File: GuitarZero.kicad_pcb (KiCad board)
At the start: 6 copper layers, 160.4 x 102.9 mm, 144 parts, among them J1 USB_A, J2 USB_B_Micro, J3 AudioJack3_SwitchT, J4 MCU_Debug, J6 Micro_SD_Card_Det_Hirose_DM3AT, SW1 SW_Push, SW2 SW_Push, SW3 SW_Push, SW4 SW_Push, SW5 SW_Push, SW6 SW_Push, U1 TPS54325, U10 FPGA_GPIO_Extra, U11 5x7 LED_matrix, U12 MCU_GPIO_Extra, U13 5x7 LED_matrix, U14 Power_Jumpers, U2 TSP54294, U3 XC7A100T-FTG256, U4 EFM32GG332, U5 S25FL127S, U6 Oscillator, U7 FPGA_JTAG_Debug, U8 PCM1754, U9 TPD_Current_Switch, Y1 Crystal_GND23

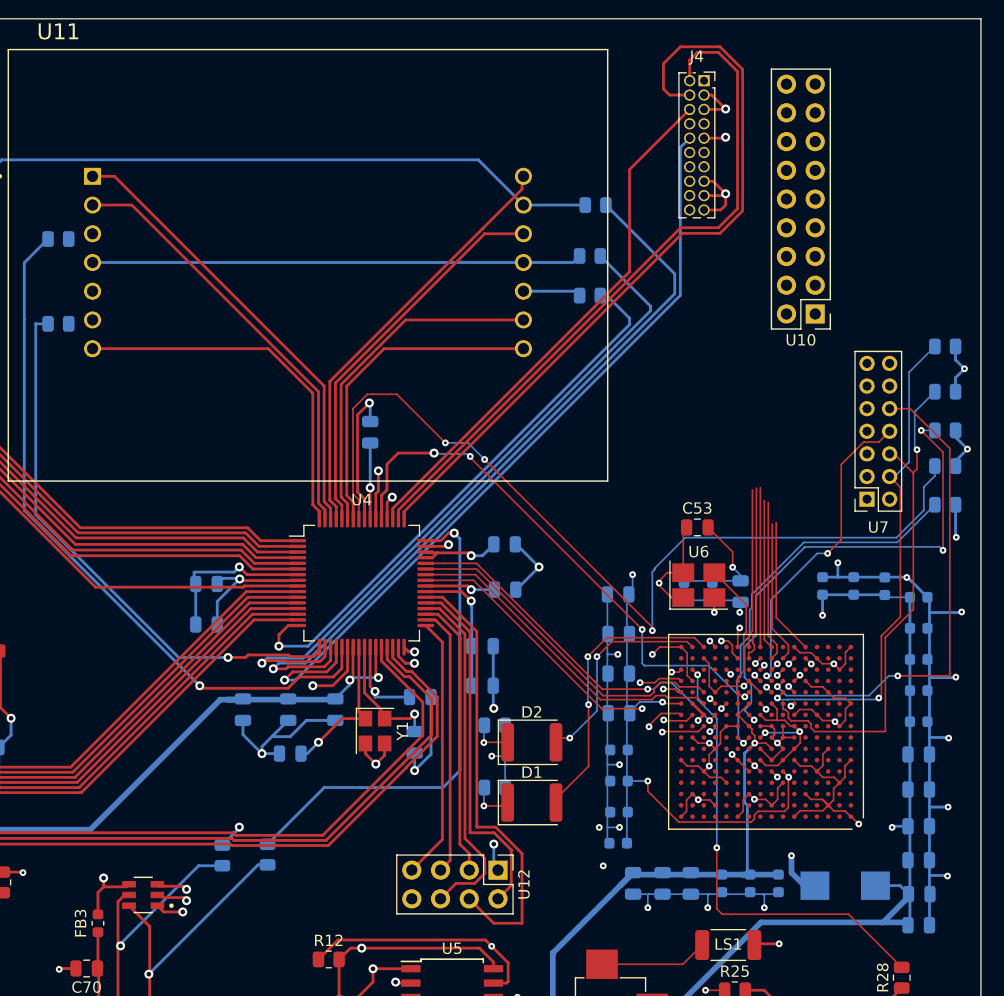
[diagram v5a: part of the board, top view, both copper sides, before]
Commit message: FInished wiring FPGA GPIO to pin headers
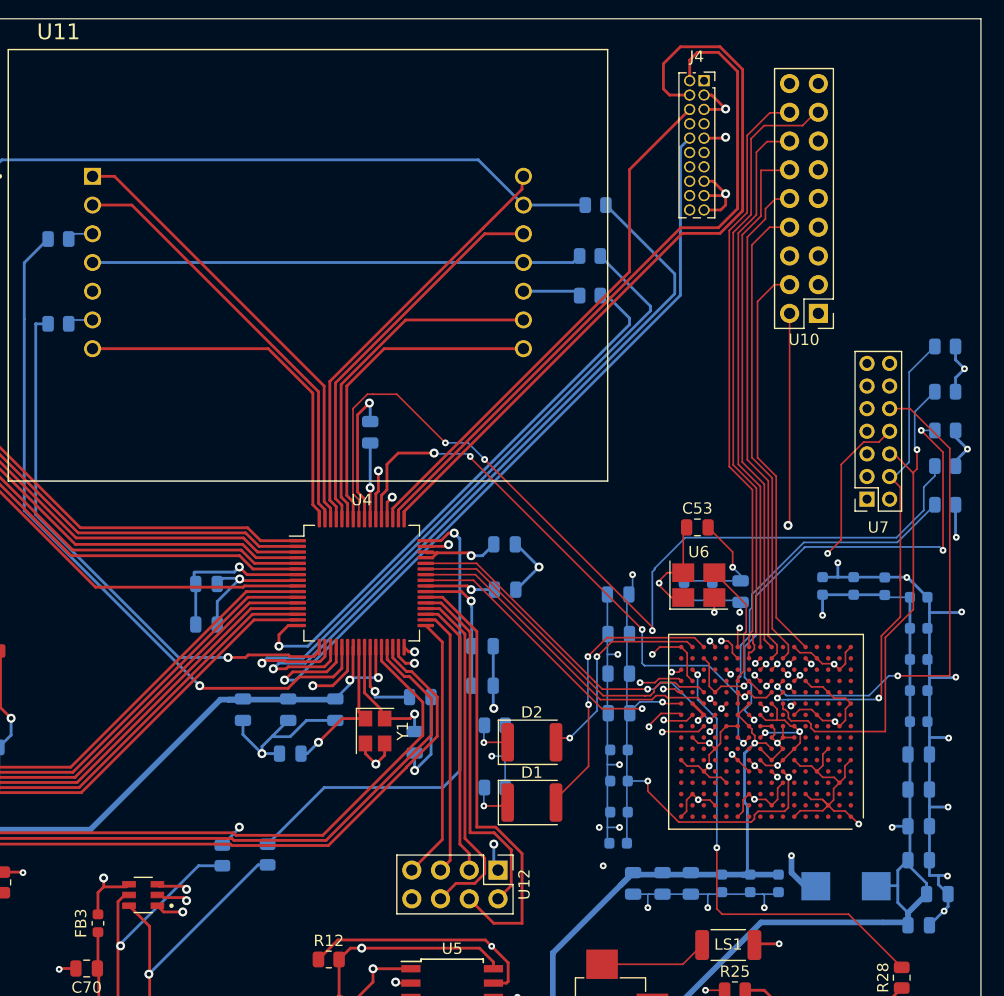
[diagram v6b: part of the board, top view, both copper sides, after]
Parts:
- moved C22 1.60 mm to (212.9, 117.5)
- moved U10 0.28 mm to (202.4, 66.2)
- moved C20 0.09 mm to (204.8, 116.8)
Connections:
- U3 pad R5: Net-(U10-GPIO_10) -> Net-(U10-GPIO_2)
- U3 pad R6: Net-(U10-GPIO_14) -> Net-(U10-GPIO_6)
- U3 pad R7: Net-(U10-GPIO_16) -> Net-(U10-GPIO_8)
- U3 pad R8: Net-(U10-GPIO_2) -> Net-(U10-GPIO_10)
- U3 pad T10: Net-(U10-GPIO_8) -> Net-(U10-GPIO_16)
- U3 pad T5: Net-(U10-GPIO_12) -> Net-(U10-GPIO_4)
- U3 pad T8: Net-(U10-GPIO_4) -> Net-(U10-GPIO_12)
- U3 pad T9: Net-(U10-GPIO_6) -> Net-(U10-GPIO_14)
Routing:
- net Net-(U10-GPIO_15): track 13.3 -> 59.8 mm
- net Net-(U10-GPIO_13): track 15.6 -> 54.6 mm
- net Net-(U10-GPIO_16): track 12.7 -> 51.2 mm
- net Net-(U10-GPIO_14): track 13.0 -> 48.3 mm, vias 1 -> 0
- net Net-(U10-GPIO_12): track 12.1 -> 46.2 mm
- net Net-(U10-GPIO_11): track 17.9 -> 51.7 mm
- net Net-(U10-GPIO_5): track 15.7 -> 48.3 mm
- net Net-(U10-GPIO_9): track 19.4 -> 49.6 mm
- net Net-(U10-GPIO_10): track 13.7 -> 43.9 mm, vias 1 -> 0
- net Net-(U10-GPIO_6): track 14.1 -> 43.9 mm, vias 0 -> 1
- net Net-(U10-GPIO_3): track 14.5 -> 43.4 mm
- net Net-(U10-GPIO_7): track 17.2 -> 45.9 mm
- net Net-(U10-GPIO_8): track 14.0 -> 42.1 mm
- net Net-(U10-GPIO_1): track 13.0 -> 39.1 mm
- net Net-(U10-GPIO_4): track 13.2 -> 35.8 mm
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
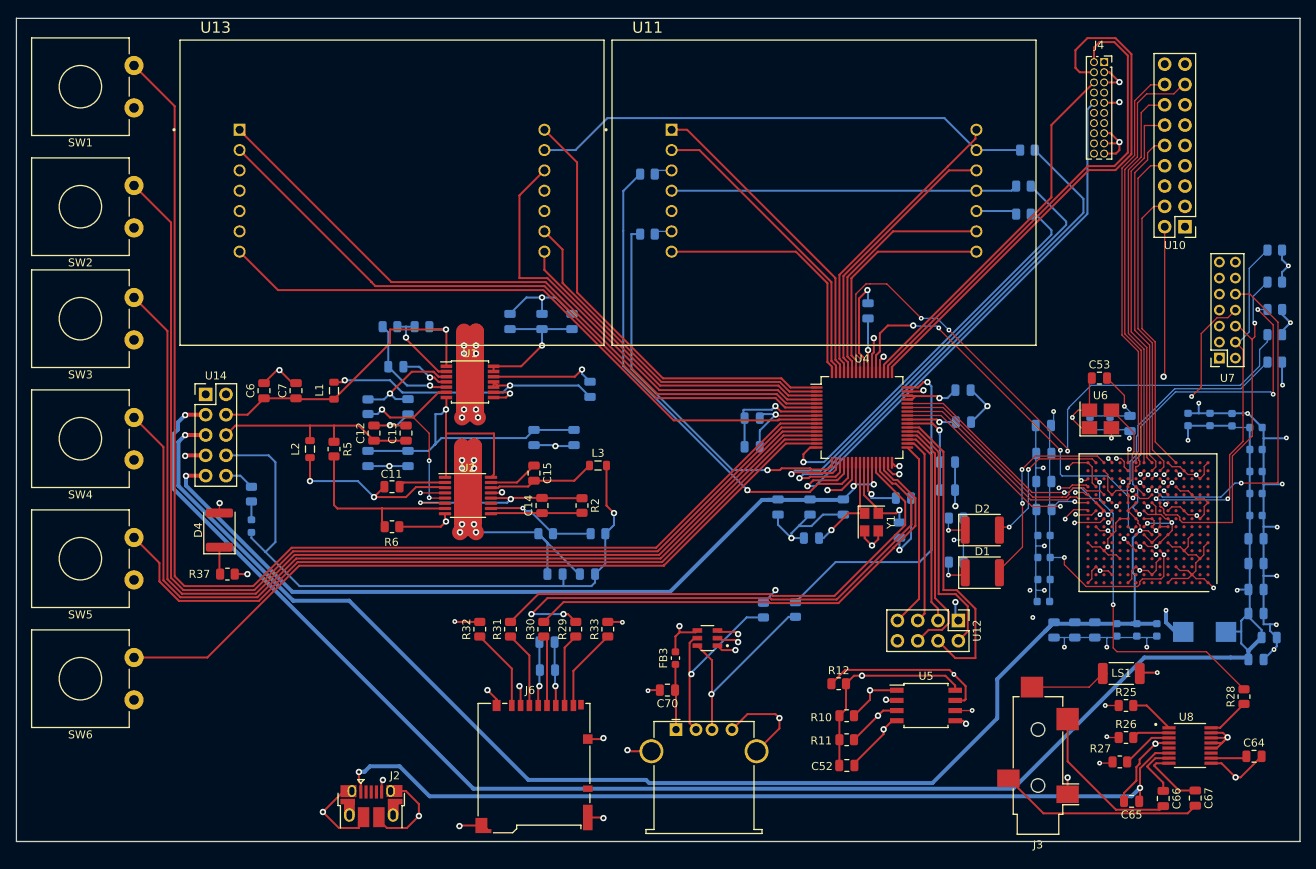
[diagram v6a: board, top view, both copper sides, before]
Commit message: Added 3.3V vias for Button 1->6
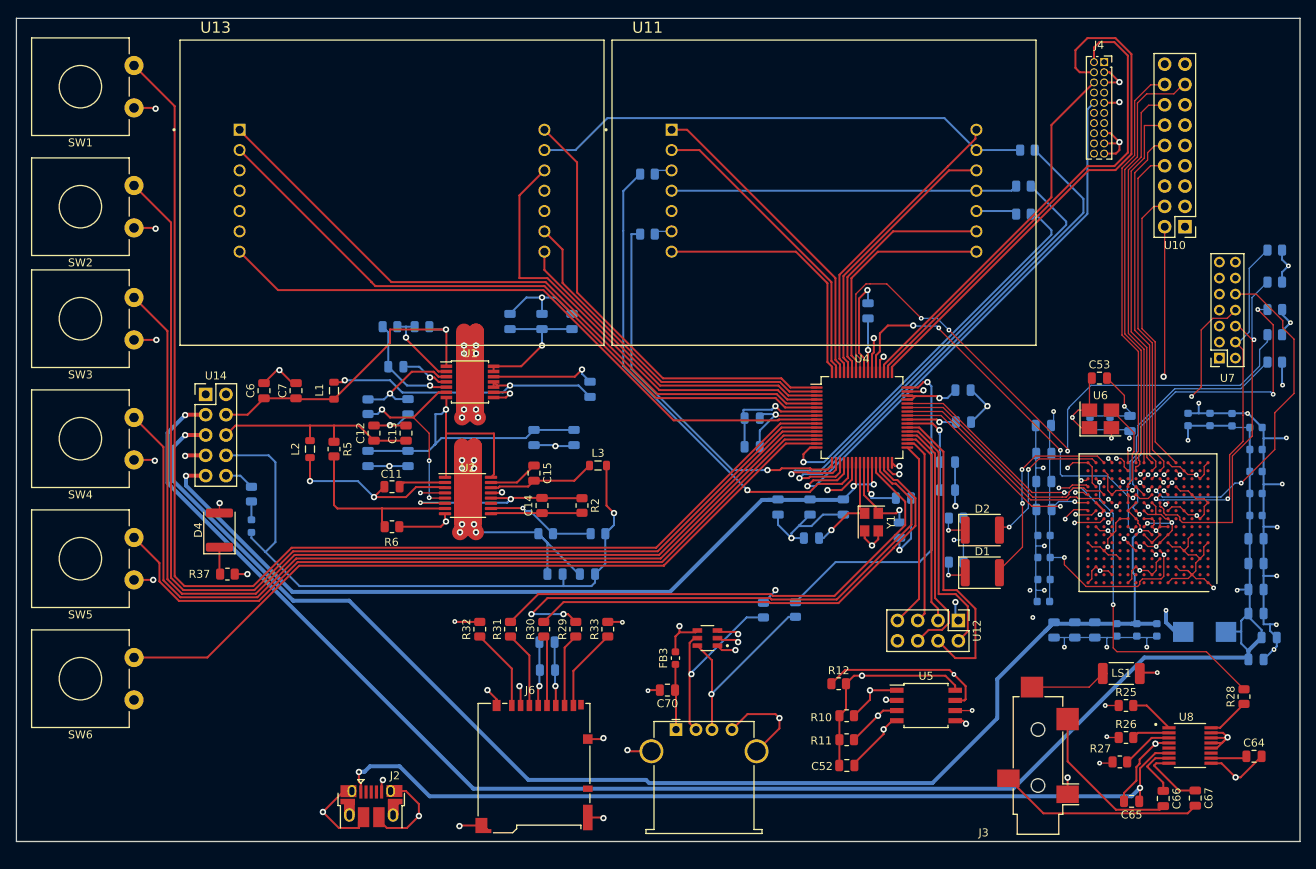
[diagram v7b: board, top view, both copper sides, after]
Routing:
- net +3.3V: track 177.3 -> 190.6 mm, vias 23 -> 28
- net +1V0: track 282.3 -> 282.8 mm
- net +1V8: track 192.4 -> 192.9 mm
- net Net-(U3C-TDI_0): track 43.8 -> 43.3 mm

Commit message: Added 1V0 layer, Increased heatsinks
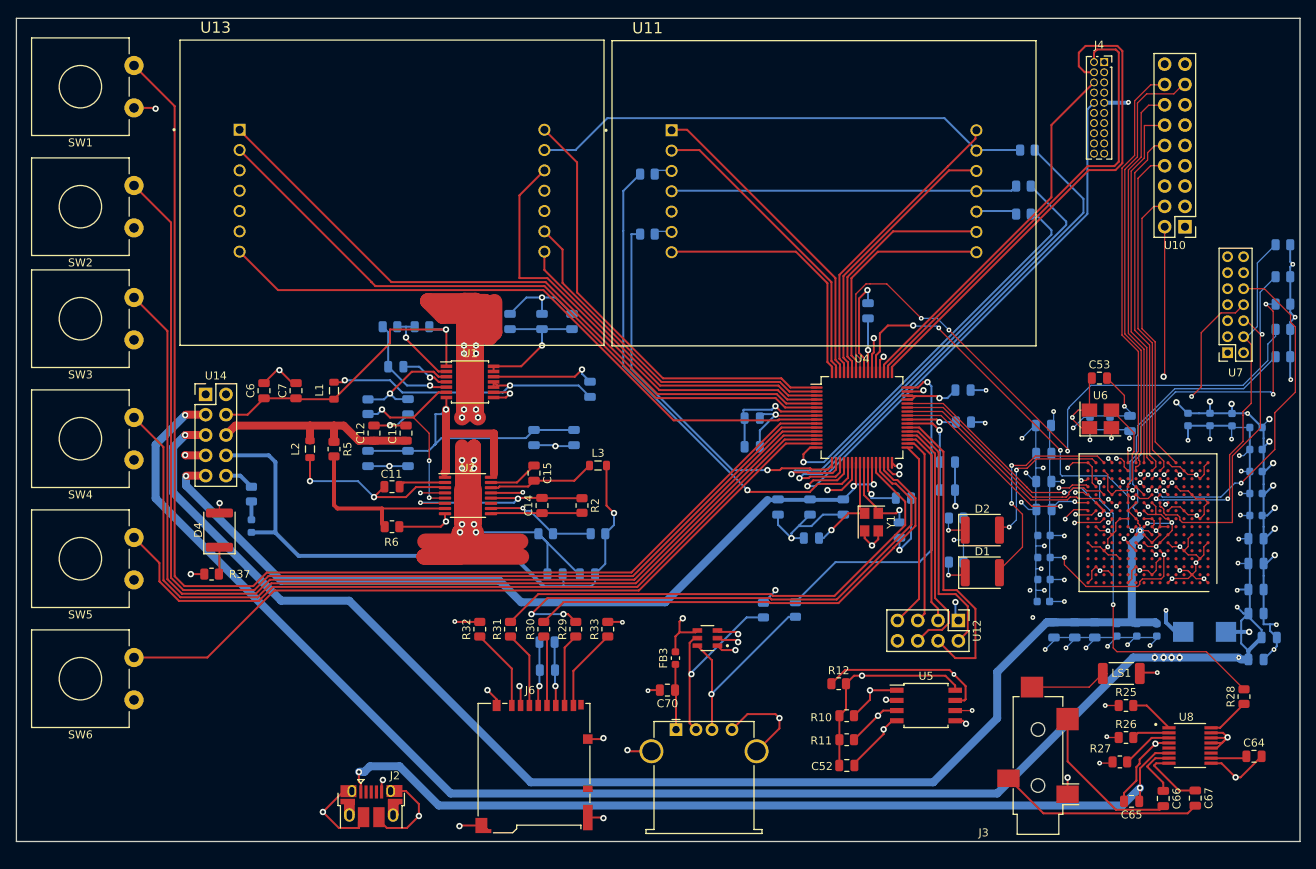
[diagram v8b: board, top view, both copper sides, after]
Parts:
- moved R37 1.98 mm to (80.7, 109.6), turned to 0 degrees
- moved R13 1.22 mm to (214.6, 68.4)
- moved R14 1.22 mm to (214.6, 72.4)
- moved R15 1.22 mm to (214.6, 75.8)
- moved R16 1.22 mm to (214.6, 79.0)
- moved R17 1.22 mm to (214.6, 82.4)
- moved U7 1.22 mm to (207.7, 81.9)
- moved U11 0.07 mm to (157.2, 61.7)
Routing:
- net GND: track 528.8 -> 601.2 mm, vias 89 -> 105
- net +1V8: track 192.9 -> 180.6 mm
- net +5V: track 289.5 -> 297.4 mm
- net +1V0: track 282.8 -> 279.1 mm, vias 8 -> 24
- net /PSU/+3.3V: track 82.2 -> 78.8 mm
- net Net-(J4-SWCLK): track 67.3 -> 64.0 mm
- net Net-(J4-SWDIO): track 61.0 -> 58.5 mm
- net +3.3V: track 190.6 -> 192.9 mm
- net Net-(D1-A): track 25.1 -> 27.2 mm
- net /FPGA/program_b: track 95.8 -> 97.1 mm
- net /FPGA/Done: track 81.3 -> 82.6 mm
- net +3.3VA: track 116.3 -> 117.3 mm
- net Net-(U2-EN2): track 26.1 -> 27.0 mm
- net Net-(D2-A): track 18.8 -> 19.6 mm
- net Net-(U3C-TMS_0): track 44.0 -> 44.6 mm
- added copper zone on In4.Cu, net +1V0
